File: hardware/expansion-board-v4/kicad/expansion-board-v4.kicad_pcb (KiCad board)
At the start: 6 copper layers, 100 x 62 mm, 174 parts, among them J1 PinHeader_2x20_P2.54mm_Vertic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, J2 U.FL_Hirose_U.FL-R-SMT-1_Vert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, J4 USB_C_Receptacle_HRO_TYPE-C-3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, J5 U.FL_Hirose_U.FL-R-SMT-1_Vert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, J6 U.FL_Hirose_U.FL-R-SMT-1_Vert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, J7 U.FL_Hirose_U.FL-R-SMT-1_Vert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, J8 U.FL_Hirose_U.FL-R-SMT-1_Vert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, J9 MX1.25WT-2P, Q2 SOT-23, Q3 SOT-23, Q4 SOT-23, Q5 SOT-23, SW2 SolderJumper-2_P1.3mm_Open_Pa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, U1 SOT-23-5, U10 QFN-48-1EP_7x7mm_P0.5mm_EP5.1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, U11 DFN-8-1EP_2x2mm_P0.5mm_EP0.86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, U12 SOT-363_SC-70-6, U14 MSOP-8_3x3mm_P0.65mm, U15 SOT-23-6, U16 SOT-363_SC-70-6, U17 SOT-363_SC-70-6, U18 SOIC-10_3.9x4.9mm_P1mm, U19 QFN-24-1EP_4x4mm_P0.5mm_EP2.6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, U2 SOT-23-5, U20 TSOT-23-6, U3 SOT-23-5, U4 BNO085_LGA-28, U5 BMP388_LGA-10, U6 LGA-16_3x3mm_P0.5mm, U7 ATGM336H_LCC-18, U8 QFN-56-1EP_7x7mm_P0.4mm_EP3.2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, U9 SOIC-8_5.3x5.3mm_P1.27mm, Y1 Crystal_SMD_3225-4Pin_3.2x2.5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, Y2 Crystal_SMD_3225-4Pin_3.2x2.5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, Y3 Crystal_SMD_3215-2Pin_3.2x1.5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

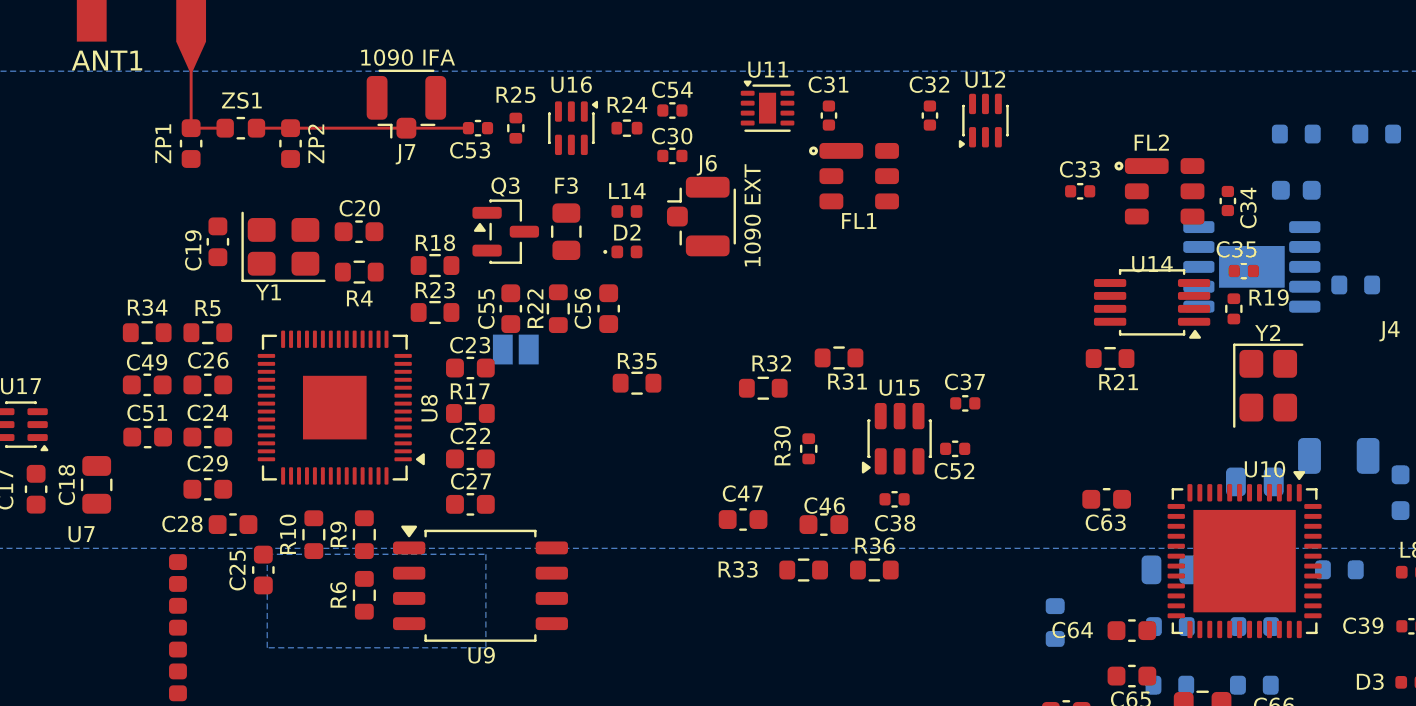
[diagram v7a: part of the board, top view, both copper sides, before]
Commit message: docs(v4): 刷新 TP 删除与 AD8319 删除的全部残留说明
## ① DEMOD0–3 / RECOVERED_CLK 的真相

这 5 条网络就是原来的 TP3–TP7。sheet_mcu.py:111 记着删 TP 的判据：
「这 7 条网络除了测试点没有第三方节点」——所以 TP 一删，它们只剩 RP2040
一端，成了悬空网。这不是漏接，是 PIO 状态机往外抛的调试位，固件不依赖。

但文档一直没说清楚，只看网表的人会以为漏接。补上：
- BOARD_TEST.md 测试点速查表加醒目提示：板上已无任何可探落点，要看用 v3.2
- PINMAP.md GPIO20–24 两行标注「V4 无落点」

## ② AD8319 删除的残留

会影响运行的数据结构（引用了已不存在的位号）：
- gen_pcb.py          SLICER 装箱区列表去掉 U13/R20
- place_fix.py        去掉 "R20": "U13" 映射
- area_budget.py      去掉 U13 面积配额
- fanout_blockers.py  芯片列表去掉 U13

文档：
- BOARD_TEST.md   接收链信号流 AD8319 → AD8313；RF_DET_OUT 探点改 R21.2
- PINMAP.md       RSSI 回读源、3V3_RF 负载清单、接收链框图、器件表、CLPF 注记
- LAYOUT_CONSTRAINTS.md §5 双封装位约束改为「U14 输入迎源、输出朝下游」；
                  框图 TJ1→U13/U14 改为 C34→U14
- REVIEW_TODO.md 历史条目标注作废

保留：gen_footprints / gen_symbols / gen_3d 里的 AD8319 封装与符号定义
（库条目，不占板位，回退时还用得上）；各脚本里记录历史事故的注释也保留。

## ③ 本轮布局固化

用户手工调整 20 件（U14 组整体西移到 slicer 一侧、晶振组重排、C33/FL2 转向）。
DRC 6 条 0 error——courtyards_overlap 与 silk_overlap 双双归零，为历轮最好；
未连接 292、parity 0、IFA 走廊 5 项测试通过。

另把 freerouting 的中间文件（freerouting.dsn / temp-freerouting.dsn）加入
.gitignore，避免误提交。
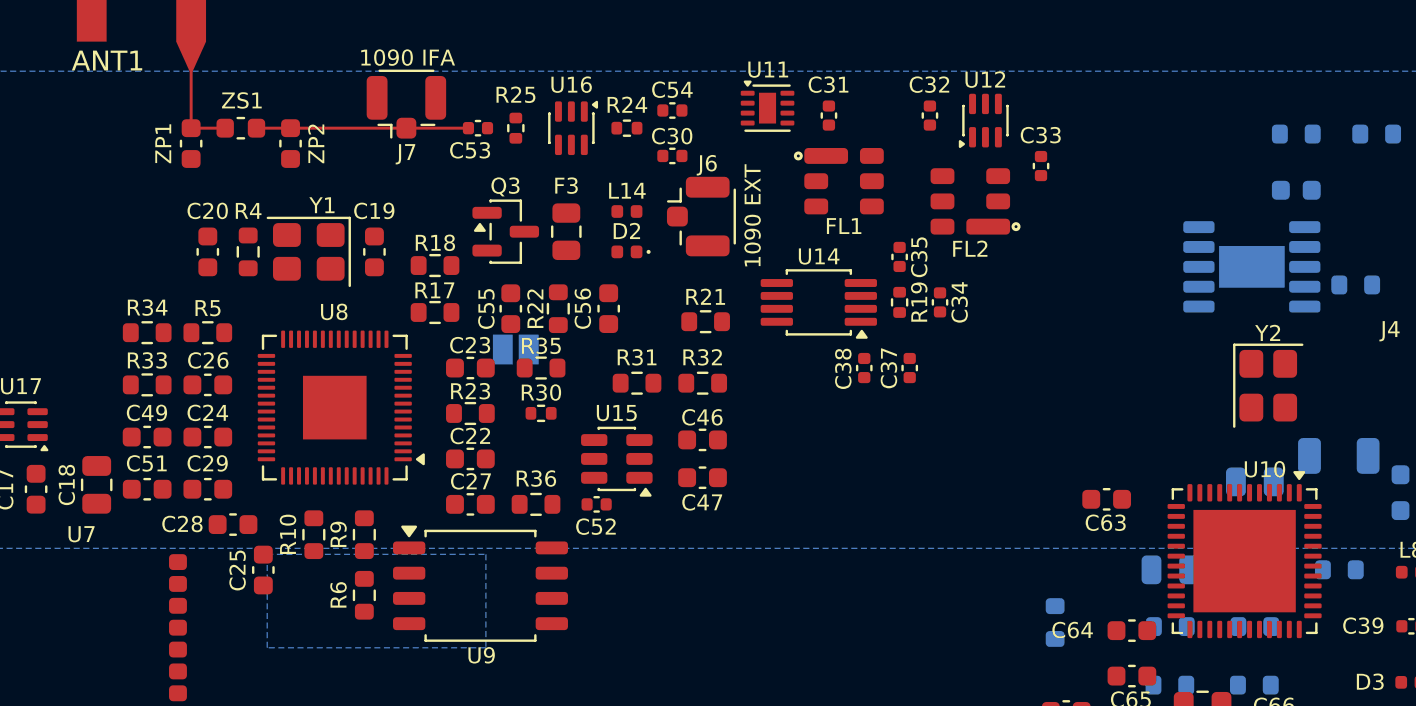
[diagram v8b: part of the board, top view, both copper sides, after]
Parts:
- moved R33 34.3 mm to (77.0, 75.8), turned to 180 degrees
- moved R21 20.4 mm to (105.1, 72.6), turned to 180 degrees
- moved C52 18.2 mm to (99.6, 81.8)
- moved R36 17.3 mm to (96.5, 81.8), turned to 180 degrees
- moved C35 17.3 mm to (114.8, 69.3), turned to 90 degrees
- moved R19 16.8 mm to (114.8, 71.6), turned to 90 degrees
- moved U14 16.8 mm to (110.7, 71.6)
- moved C34 15.3 mm to (116.8, 71.6)
- moved U15 14.3 mm to (100.6, 79.5), turned to 180 degrees
- moved R30 13.6 mm to (96.8, 77.2), turned to 180 degrees
- moved R31 10.2 mm to (101.6, 75.7)
- moved FL2 9.79 mm to (118.4, 66.5), turned to 180 degrees
- moved C19 7.89 mm to (88.4, 69.1), turned to -90 degrees
- moved C20 7.67 mm to (80.0, 69.1), turned to 90 degrees
- moved C46 7.44 mm to (104.9, 78.5), turned to 0 degrees
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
